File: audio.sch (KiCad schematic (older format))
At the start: 94 parts, among them CN1 LEFT_JOY, CN2 RIGHT_JOY, CN3 RIGHT, CN4 LEFT, Q301 2N3906, Q321 MPF102, Q331 MPF102, U14 LF347, U15 74LS157, U3 PAULA, U38 MC1488

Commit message: Almost there :)
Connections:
- net ~DKRD: now also R305.2
- net ~RXD: no longer R305.2
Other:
- moved on the sheet: R305
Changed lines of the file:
@@
 Sheet 5 14
 Title "Rämixx500"
-Date "2019-05-23"
+Date "2019-06-23"
 Rev "1git"
 Comp "SukkoPera"
@@
 ~INT2
 Wire Wire Line
-	3875 6155 4050 6155
-Wire Wire Line
 	3875 6305 4270 6305
 Text GLabel 4270 6155 2    50   Input ~ 0
@@
 ~TXD
 Wire Wire Line
-	3875 6705 4270 6705
+	3875 6705 4040 6705
 Wire Wire Line
 	3875 6855 4270 6855
@@
 L Device:R R305
 U 1 1 5E111042
-P 4300 5945
-F 0 "R305" V 4215 5845 50  0000 L CNN
-F 1 "1k" V 4300 5900 50  0000 L CNN
-F 2 "Raemixx500:R_Axial_DIN0309_L9.0mm_D3.2mm_P12.70mm_Horizontal" V 4230 5945 50  0001 C CNN
-F 3 "~" H 4300 5945 50  0001 C CNN
-	1    4300 5945
+P 4290 6495
+F 0 "R305" V 4205 6395 50  0000 L CNN
+F 1 "1k" V 4290 6450 50  0000 L CNN
+F 2 "Raemixx500:R_Axial_DIN0309_L9.0mm_D3.2mm_P12.70mm_Horizontal" V 4220 6495 50  0001 C CNN
+F 3 "~" H 4290 6495 50  0001 C CNN
+	1    4290 6495
 	0    1    1    0
 $EndComp
@@
 L power:VCC #PWR0159
 U 1 1 5E4D343F
-P 4650 5875
-F 0 "#PWR0159" H 4650 5725 50  0001 C CNN
-F 1 "VCC" H 4667 6048 50  0000 C CNN
-F 2 "" H 4650 5875 50  0001 C CNN
-F 3 "" H 4650 5875 50  0001 C CNN
-	1    4650 5875
-	1    0    0    -1
-$EndComp
-Wire Wire Line
-	4450 5945 4650 5945
-Wire Wire Line
-	4650 5945 4650 5875
-Wire Wire Line
-	4150 5945 4050 5945
-Wire Wire Line
-	4050 5945 4050 6155
-Connection ~ 4050 6155
-Wire Wire Line
-	4050 6155 4270 6155
+P 4640 6425
+F 0 "#PWR0159" H 4640 6275 50  0001 C CNN
+F 1 "VCC" H 4657 6598 50  0000 C CNN
+F 2 "" H 4640 6425 50  0001 C CNN
+F 3 "" H 4640 6425 50  0001 C CNN
+	1    4640 6425
+	1    0    0    -1
+$EndComp
+Wire Wire Line
+	4440 6495 4640 6495
+Wire Wire Line
+	4640 6495 4640 6425
+Wire Wire Line
+	4140 6495 4040 6495
+Wire Wire Line
+	4040 6495 4040 6705
 $Comp
 L Device:R R307
@@
 Wire Wire Line
 	5995 5030 7280 5030
+Connection ~ 4040 6705
+Wire Wire Line
+	4040 6705 4270 6705
+Wire Wire Line
+	3875 6155 4270 6155
 Wire Bus Line
 	1955 4305 1955 4505

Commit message: Fix shielding of D-Sub connectors
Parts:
- CN1, CN2: footprint w_conn_d-sub:DB_9M -> Raemixx500:DB_9M
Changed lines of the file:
@@
 F 0 "CN1" H 8775 1608 50  0000 C CNN
 F 1 "LEFT_JOY" H 8775 1699 50  0000 C CNN
-F 2 "w_conn_d-sub:DB_9M" H 8775 2300 50  0001 C CNN
+F 2 "Raemixx500:DB_9M" H 8775 2300 50  0001 C CNN
 F 3 " ~" H 8775 2300 50  0001 C CNN
 	1    8775 2300
@@
 F 0 "CN2" H 8775 3838 50  0000 C CNN
 F 1 "RIGHT_JOY" H 8775 3929 50  0000 C CNN
-F 2 "w_conn_d-sub:DB_9M" H 8775 4530 50  0001 C CNN
+F 2 "Raemixx500:DB_9M" H 8775 4530 50  0001 C CNN
 F 3 " ~" H 8775 4530 50  0001 C CNN
 	1    8775 4530

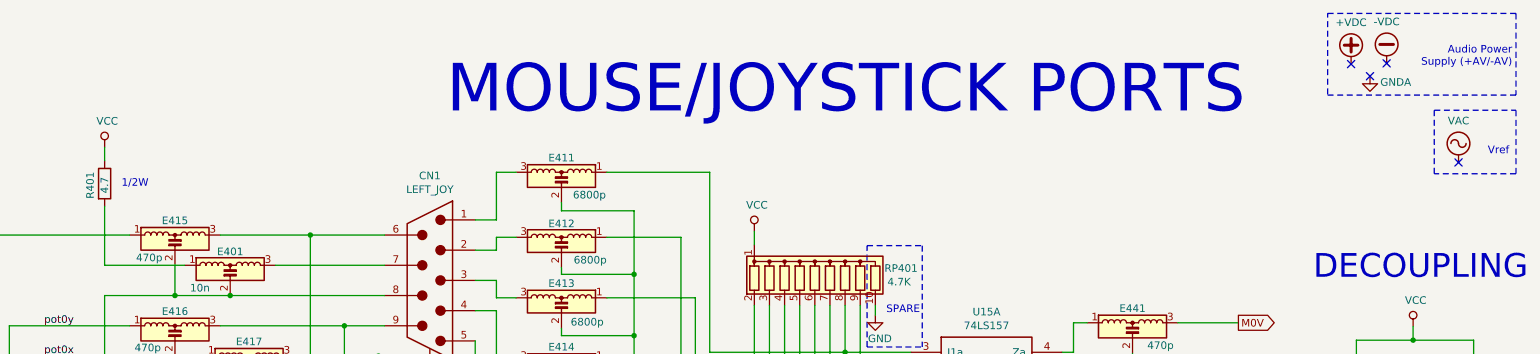
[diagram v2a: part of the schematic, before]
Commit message: Fix a lot of ERC/DRC errors
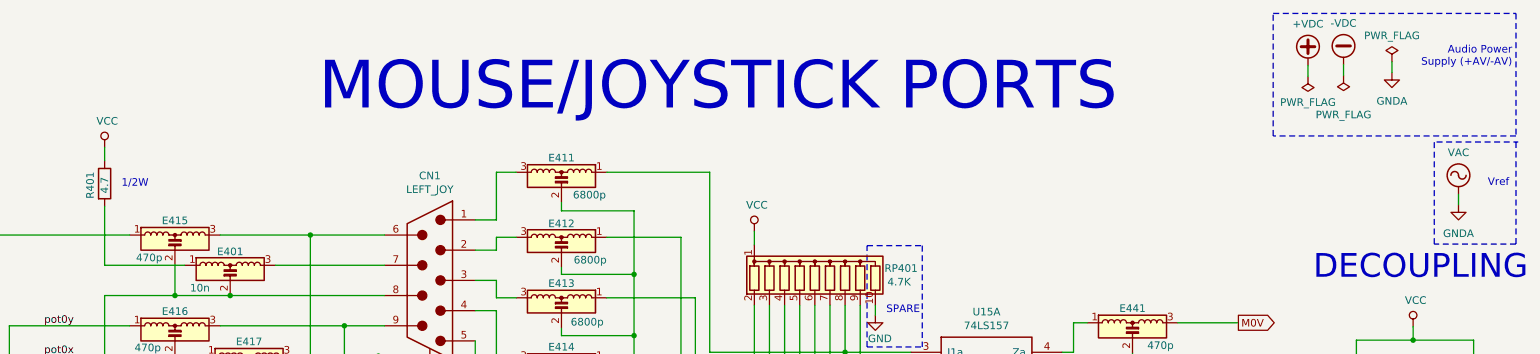
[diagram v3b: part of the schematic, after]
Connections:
- net VAC is gone; now on net GNDA: C305.1, C306.1, R303.1, R304.2, U14.10 (+), U14.12 (+)
- no-connect marks 4 -> 0
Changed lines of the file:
@@
 EESchema Schematic File Version 4
-LIBS:Raemix500-cache
-EELAYER 29 0
+EELAYER 30 0
 EELAYER END
 $Descr A3 16535 11693
@@
 Sheet 5 14
 Title "Rämixx500"
-Date "2019-06-23"
+Date "2020-04-04"
 Rev "1git"
 Comp "SukkoPera"
@@
 	1    0    0    -1
 $EndComp
-NoConn ~ 15100 865
 Text Notes 15930 890  2    50   ~ 0
 Audio Power\nSupply (+AV/-AV)
 Wire Notes Line
-	14710 535  15955 535
+	14350 535  15955 535
 Wire Notes Line
-	15955 535  15955 1075
+	15955 535  15955 1360
 Wire Notes Line
-	15955 1075 14710 1075
+	15955 1345 14350 1345
 Wire Notes Line
-	14710 1070 14710 535
+	14350 1345 14350 525
 $Comp
 L power:GNDA #PWR0132
 U 1 1 5D31919F
-P 14990 950
-F 0 "#PWR0132" H 14990 700 50  0001 C CNN
-F 1 "GNDA" H 15160 910 50  0000 C CNN
-F 2 "" H 14990 950 50  0001 C CNN
-F 3 "" H 14990 950 50  0001 C CNN
-	1    14990 950
-	1    0    0    -1
-$EndComp
-NoConn ~ 14990 950
+P 15135 925
+F 0 "#PWR0132" H 15135 675 50  0001 C CNN
+F 1 "GNDA" H 15135 735 50  0000 C CNN
+F 2 "" H 15135 925 50  0001 C CNN
+F 3 "" H 15135 925 50  0001 C CNN
+	1    15135 925
+	1    0    0    -1
+$EndComp
 $Comp
 L Device:EMI_Filter_LCL E416
@@
 L power:VAC #PWR0147
 U 1 1 5DBE05B3
-P 15575 1520
-F 0 "#PWR0147" H 15575 1420 50  0001 C CNN
-F 1 "VAC" H 15575 1795 50  0000 C CNN
-F 2 "" H 15575 1520 50  0001 C CNN
-F 3 "" H 15575 1520 50  0001 C CNN
-	1    15575 1520
-	1    0    0    -1
-$EndComp
-NoConn ~ 15575 1520
-Text Notes 15910 1475 2    50   ~ 0
+P 15575 1730
+F 0 "#PWR0147" H 15575 1630 50  0001 C CNN
+F 1 "VAC" H 15575 2005 50  0000 C CNN
+F 2 "" H 15575 1730 50  0001 C CNN
+F 3 "" H 15575 1730 50  0001 C CNN
+	1    15575 1730
+	1    0    0    -1
+$EndComp
+Text Notes 15910 1685 2    50   ~ 0
 Vref
 $Comp
@@
 Text Notes 15090 6570 2    315  ~ 0
 AUDIO FILTERS
-Text Notes 14165 1225 2    315  ~ 0
+Text Notes 13320 1205 2    315  ~ 0
 MOUSE/JOYSTICK PORTS
 $Comp
@@
 	6870 6920 7175 6920
 Wire Notes Line
-	15415 1175 15955 1175
+	15430 1385 15970 1385
 Wire Notes Line
-	15955 1175 15955 1595
+	15955 1385 15955 2075
 Wire Notes Line
-	15955 1595 15415 1595
+	15955 2060 15415 2060
 Wire Notes Line
-	15415 1595 15415 1175
+	15415 2060 15415 1385
 Text Notes 9045 10220 2    50   ~ 0
 This whole circuit has some\ndifferent values on A600.
@@
 L power:-VDC #PWR0216
 U 1 1 5DF41869
-P 15100 865
-F 0 "#PWR0216" H 15100 765 50  0001 C CNN
-F 1 "-VDC" H 15100 1140 50  0000 C CNN
-F 2 "" H 15100 865 50  0001 C CNN
-F 3 "" H 15100 865 50  0001 C CNN
-	1    15100 865
+P 14815 875
+F 0 "#PWR0216" H 14815 775 50  0001 C CNN
+F 1 "-VDC" H 14815 1150 50  0000 C CNN
+F 2 "" H 14815 875 50  0001 C CNN
+F 3 "" H 14815 875 50  0001 C CNN
+	1    14815 875
 	1    0    0    -1
 $EndComp
@@
 L power:+VDC #PWR0217
 U 1 1 5DF419B8
-P 14865 870
-F 0 "#PWR0217" H 14865 770 50  0001 C CNN
-F 1 "+VDC" H 14865 1145 50  0000 C CNN
-F 2 "" H 14865 870 50  0001 C CNN
-F 3 "" H 14865 870 50  0001 C CNN
-	1    14865 870
-	1    0    0    -1
-$EndComp
-NoConn ~ 14865 870
+P 14580 880
+F 0 "#PWR0217" H 14580 780 50  0001 C CNN
+F 1 "+VDC" H 14580 1155 50  0000 C CNN
+F 2 "" H 14580 880 50  0001 C CNN
+F 3 "" H 14580 880 50  0001 C CNN
+	1    14580 880
+	1    0    0    -1
+$EndComp
 $Comp
 L power:-VDC #PWR0218
@@
 Wire Wire Line
 	3875 6155 4270 6155
+$Comp
+L power:PWR_FLAG #FLG0103
+U 1 1 5EE75F30
+P 15135 855
+F 0 "#FLG0103" H 15135 930 50  0001 C CNN
+F 1 "PWR_FLAG" H 15135 1028 50  0000 C CNN
+F 2 "" H 15135 855 50  0001 C CNN
+F 3 "~" H 15135 855 50  0001 C CNN
+	1    15135 855
+	1    0    0    -1
+$EndComp
+Wire Wire Line
+	15135 925  15135 855
+$Comp
+L power:PWR_FLAG #FLG0104
+U 1 1 5EF3EBCB
+P 14815 945
+F 0 "#FLG0104" H 14815 1020 50  0001 C CNN
+F 1 "PWR_FLAG" H 14815 1205 50  0000 C CNN
+F 2 "" H 14815 945 50  0001 C CNN
+F 3 "~" H 14815 945 50  0001 C CNN
+	1    14815 945
+	-1   0    0    1
+$EndComp
+Wire Wire Line
+	14815 875  14815 945
+$Comp
+L power:PWR_FLAG #FLG0105
+U 1 1 5EF849F2
+P 14580 950
+F 0 "#FLG0105" H 14580 1025 50  0001 C CNN
+F 1 "PWR_FLAG" H 14580 1123 50  0000 C CNN
+F 2 "" H 14580 950 50  0001 C CNN
+F 3 "~" H 14580 950 50  0001 C CNN
+	1    14580 950
+	-1   0    0    1
+$EndComp
+Wire Wire Line
+	14580 880  14580 950
+$Comp
+L power:GNDA #PWR0270
+U 1 1 5F2DFC32
+P 15575 1800
+F 0 "#PWR0270" H 15575 1550 50  0001 C CNN
+F 1 "GNDA" H 15575 1610 50  0000 C CNN
+F 2 "" H 15575 1800 50  0001 C CNN
+F 3 "" H 15575 1800 50  0001 C CNN
+	1    15575 1800
+	1    0    0    -1
+$EndComp
+Wire Wire Line
+	15575 1800 15575 1730
 Wire Bus Line
 	1955 4305 1955 4505

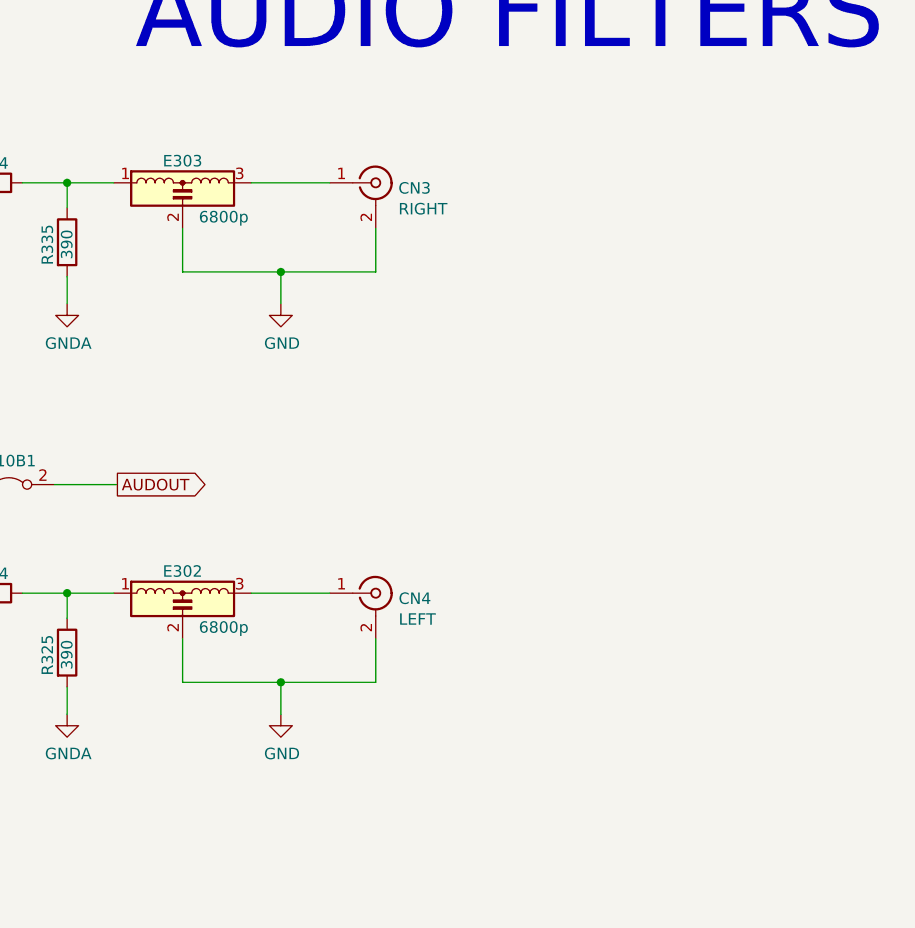
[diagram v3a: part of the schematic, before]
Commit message: Replace audio/composite jacks with A600's - This means PCB IS READY! Still need to fix the silkscreen though...
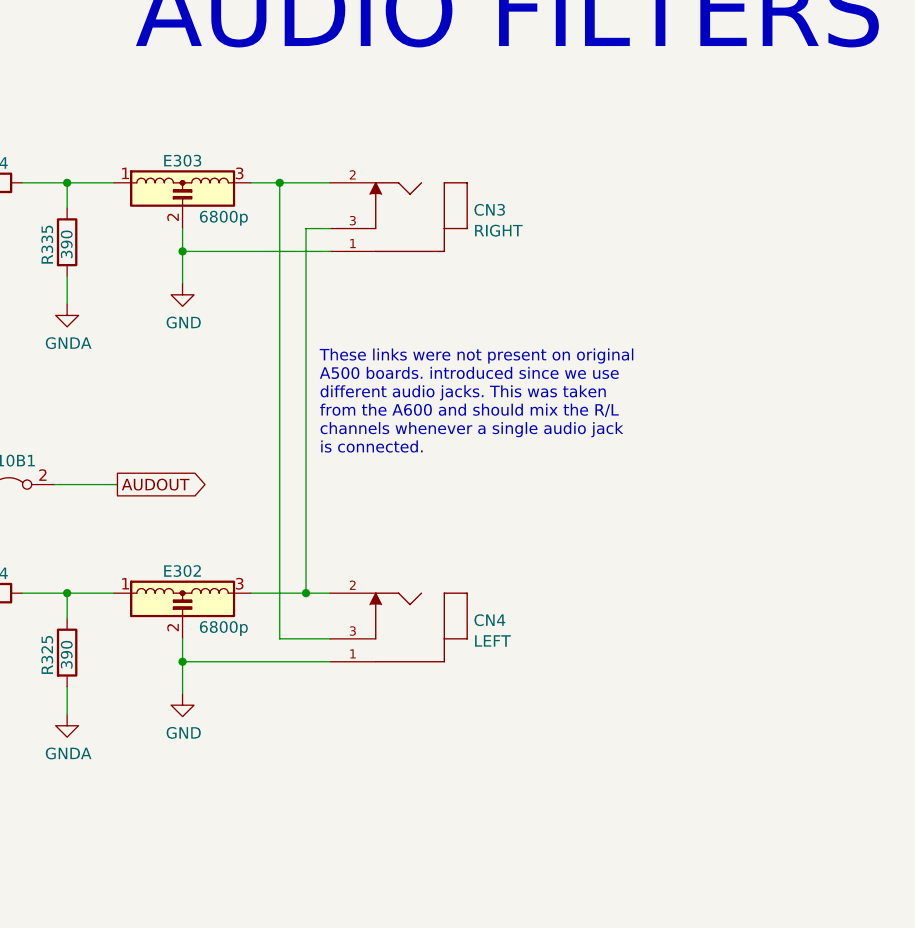
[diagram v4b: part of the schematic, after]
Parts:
- removed CN3: RIGHT, w_conn_av:rca_red, symbol Connector:Conn_Coaxial
- removed CN4: LEFT, w_conn_av:rca_white, symbol Connector:Conn_Coaxial
- added CN3: RIGHT, Raemixx500:SWITCHCRAFT_PJRAN1X1U01X, symbol PJRAN1X1U01X:PJRAN1X1U01X
- added CN4: LEFT, Raemixx500:SWITCHCRAFT_PJRAN1X1U01X, symbol PJRAN1X1U01X:PJRAN1X1U01X
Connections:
- net GND: now also CN3.1, CN4.1
- net at E302.3: now also CN3.3, CN4.2
- net at E303.3: now also CN3.2, CN4.3
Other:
- note added: "These links were not present on original\nA500 boards. introduced since we use\ndifferent audio jacks. This was taken\nfrom the A600 and should mix the R/L\nchannels whenever a single audio jack\nis connected."
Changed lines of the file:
@@
 Wire Wire Line
 	11515 9445 11515 9325
-$Comp
-L Connector:Conn_Coaxial CN4
-U 1 1 5DB6BA04
-P 12865 8915
-F 0 "CN4" H 12965 8891 50  0000 L CNN
-F 1 "LEFT" H 12965 8800 50  0000 L CNN
-F 2 "w_conn_av:rca_white" H 12865 8915 50  0001 C CNN
-F 3 " ~" H 12865 8915 50  0001 C CNN
-	1    12865 8915
-	1    0    0    -1
-$EndComp
-Wire Wire Line
-	12020 9115 12020 9305
-Wire Wire Line
-	12020 9305 12450 9305
-Wire Wire Line
-	12865 9305 12865 9115
-$Comp
-L power:GND #PWR0146
-U 1 1 5DB828C1
-P 12450 9445
-F 0 "#PWR0146" H 12450 9195 50  0001 C CNN
-F 1 "GND" H 12455 9272 50  0000 C CNN
-F 2 "" H 12450 9445 50  0001 C CNN
-F 3 "" H 12450 9445 50  0001 C CNN
-	1    12450 9445
-	1    0    0    -1
-$EndComp
-Wire Wire Line
-	12450 9445 12450 9305
-Connection ~ 12450 9305
-Wire Wire Line
-	12450 9305 12865 9305
-Wire Wire Line
-	12320 8915 12665 8915
+Wire Wire Line
+	12020 9115 12020 9215
 $Comp
 L power:VAC #PWR0147
@@
 Wire Wire Line
 	11515 7650 11515 7530
-$Comp
-L Connector:Conn_Coaxial CN3
-U 1 1 5DD9A1DF
-P 12865 7120
-F 0 "CN3" H 12964 7096 50  0000 L CNN
-F 1 "RIGHT" H 12964 7005 50  0000 L CNN
-F 2 "w_conn_av:rca_red" H 12865 7120 50  0001 C CNN
-F 3 " ~" H 12865 7120 50  0001 C CNN
-	1    12865 7120
-	1    0    0    -1
-$EndComp
-Wire Wire Line
-	12020 7320 12020 7510
-Wire Wire Line
-	12020 7510 12450 7510
-Wire Wire Line
-	12865 7510 12865 7320
-$Comp
-L power:GND #PWR0151
-U 1 1 5DD9A1E8
-P 12450 7650
-F 0 "#PWR0151" H 12450 7400 50  0001 C CNN
-F 1 "GND" H 12455 7477 50  0000 C CNN
-F 2 "" H 12450 7650 50  0001 C CNN
-F 3 "" H 12450 7650 50  0001 C CNN
-	1    12450 7650
-	1    0    0    -1
-$EndComp
-Wire Wire Line
-	12450 7650 12450 7510
-Connection ~ 12450 7510
-Wire Wire Line
-	12450 7510 12865 7510
-Wire Wire Line
-	12320 7120 12665 7120
+Wire Wire Line
+	12320 7120 12445 7120
 $Comp
 L power:VAC #PWR0152
@@
 Wire Wire Line
 	15575 1800 15575 1730
+$Comp
+L PJRAN1X1U01X:PJRAN1X1U01X CN3
+U 1 1 5F7C1CDB
+P 12965 7320
+F 0 "CN3" H 12637 7400 50  0000 R CNN
+F 1 "RIGHT" H 12637 7309 50  0000 R CNN
+F 2 "Raemixx500:SWITCHCRAFT_PJRAN1X1U01X" H 12965 7320 50  0001 L BNN
+F 3 "A" H 12965 7320 50  0001 L BNN
+F 4 "Switchcraft" H 12965 7320 50  0001 L BNN "Field4"
+F 5 "13mm" H 12965 7320 50  0001 L BNN "Field5"
+F 6 "Manufacturer Recommendations" H 12965 7320 50  0001 L BNN "Field6"
+	1    12965 7320
+	-1   0    0    -1
+$EndComp
+Wire Wire Line
+	12320 8915 12560 8915
+$Comp
+L PJRAN1X1U01X:PJRAN1X1U01X CN4
+U 1 1 5FA7359A
+P 12965 9115
+F 0 "CN4" H 12637 9195 50  0000 R CNN
+F 1 "LEFT" H 12637 9104 50  0000 R CNN
+F 2 "Raemixx500:SWITCHCRAFT_PJRAN1X1U01X" H 12965 9115 50  0001 L BNN
+F 3 "A" H 12965 9115 50  0001 L BNN
+F 4 "Switchcraft" H 12965 9115 50  0001 L BNN "Field4"
+F 5 "13mm" H 12965 9115 50  0001 L BNN "Field5"
+F 6 "Manufacturer Recommendations" H 12965 9115 50  0001 L BNN "Field6"
+	1    12965 9115
+	-1   0    0    -1
+$EndComp
+Wire Wire Line
+	12020 9355 12020 9215
+$Comp
+L power:GND #PWR0146
+U 1 1 5FA735A5
+P 12020 9355
+F 0 "#PWR0146" H 12020 9105 50  0001 C CNN
+F 1 "GND" H 12025 9182 50  0000 C CNN
+F 2 "" H 12020 9355 50  0001 C CNN
+F 3 "" H 12020 9355 50  0001 C CNN
+	1    12020 9355
+	1    0    0    -1
+$EndComp
+Wire Wire Line
+	12665 7320 12560 7320
+Wire Wire Line
+	12560 7320 12560 8915
+Connection ~ 12560 8915
+Wire Wire Line
+	12560 8915 12665 8915
+Connection ~ 12020 9215
+Wire Wire Line
+	12020 9215 12665 9215
+Wire Wire Line
+	12020 7320 12020 7420
+$Comp
+L power:GND #PWR0151
+U 1 1 5DD9A1E8
+P 12020 7560
+F 0 "#PWR0151" H 12020 7310 50  0001 C CNN
+F 1 "GND" H 12025 7387 50  0000 C CNN
+F 2 "" H 12020 7560 50  0001 C CNN
+F 3 "" H 12020 7560 50  0001 C CNN
+	1    12020 7560
+	1    0    0    -1
+$EndComp
+Wire Wire Line
+	12020 7560 12020 7420
+Connection ~ 12020 7420
+Wire Wire Line
+	12020 7420 12665 7420
+Wire Wire Line
+	12665 9115 12445 9115
+Wire Wire Line
+	12445 9115 12445 7120
 Wire Bus Line
 	1955 4305 1955 4505
@@
 Wire Bus Line
 	1955 4705 1955 6205
+Connection ~ 12445 7120
+Wire Wire Line
+	12445 7120 12665 7120
+Text Notes 12620 8315 0    50   ~ 0
+These links were not present on original\nA500 boards. introduced since we use\ndifferent audio jacks. This was taken\nfrom the A600 and should mix the R/L\nchannels whenever a single audio jack\nis connected.
 $EndSCHEMATC

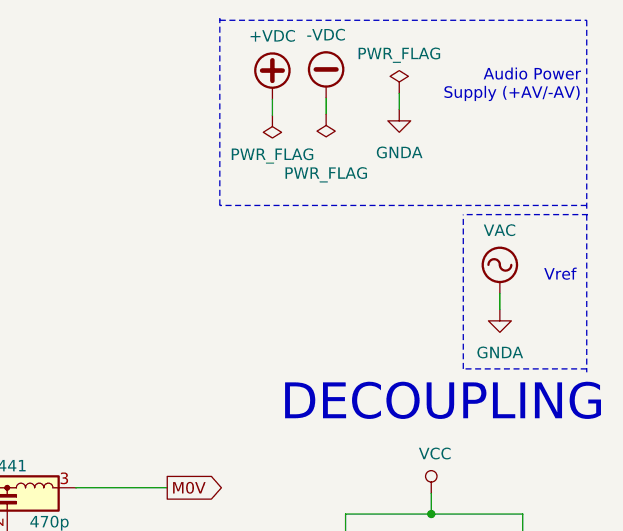
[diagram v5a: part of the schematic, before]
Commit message: Erm, fix a huge mistake in the audio part and some refinements
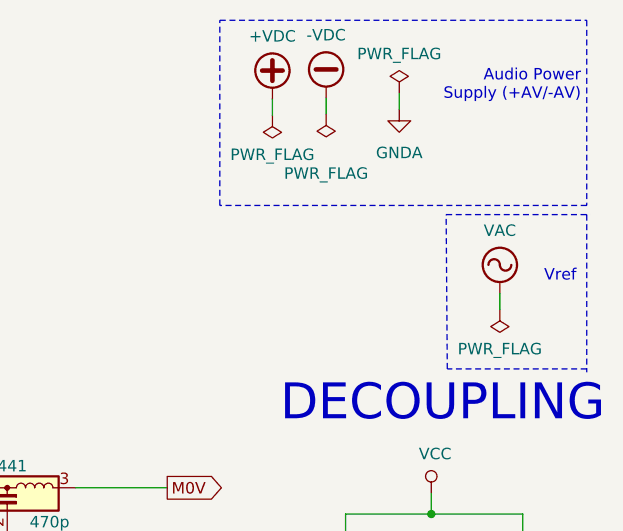
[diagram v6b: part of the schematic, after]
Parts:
- C303, C304: footprint Capacitor_THT:CP_Radial_D5.0mm_P2.00mm -> Capacitor_THT:CP_Radial_D5.0mm_P2.50mm
- C306: footprint Capacitor_THT:CP_Radial_D8.0mm_P5.00mm -> Capacitor_THT:CP_Radial_D5.0mm_P2.50mm
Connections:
- net GNDA: no longer C305.1, C306.1, R303.1, R304.2, U14.10 (+), U14.12 (+)
- new net VAC: C305.1, C306.1, R303.1, R304.2, U14.10 (+), U14.12 (+)
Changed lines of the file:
@@
 	14350 535  15955 535
 Wire Notes Line
-	15955 535  15955 1360
+	15955 535  15955 1345
 Wire Notes Line
 	15955 1345 14350 1345
 Wire Notes Line
-	14350 1345 14350 525
+	14350 1345 14350 535
 $Comp
 L power:GNDA #PWR0132
@@
 	6870 6920 7175 6920
 Wire Notes Line
-	15430 1385 15970 1385
+	15340 1385 15970 1385
 Wire Notes Line
 	15955 1385 15955 2075
 Wire Notes Line
-	15955 2060 15415 2060
+	15955 2060 15345 2060
 Wire Notes Line
-	15415 2060 15415 1385
+	15345 2060 15340 1385
 Text Notes 9045 10220 2    50   ~ 0
 This whole circuit has some\ndifferent values on A600.
@@
 F 0 "C306" H 4380 2161 50  0000 L CNN
 F 1 "10u" H 4380 2070 50  0000 L CNN
-F 2 "Capacitor_THT:CP_Radial_D8.0mm_P5.00mm" H 4265 2115 50  0001 C CNN
+F 2 "Capacitor_THT:CP_Radial_D5.0mm_P2.50mm" H 4265 2115 50  0001 C CNN
 F 3 "~" H 4265 2115 50  0001 C CNN
 	1    4265 2115
@@
 F 0 "C303" H 2175 9561 50  0000 L CNN
 F 1 "22u" H 2175 9470 50  0000 L CNN
-F 2 "Capacitor_THT:CP_Radial_D5.0mm_P2.00mm" H 2060 9515 50  0001 C CNN
+F 2 "Capacitor_THT:CP_Radial_D5.0mm_P2.50mm" H 2060 9515 50  0001 C CNN
 F 3 "~" H 2060 9515 50  0001 C CNN
 	1    2060 9515
@@
 F 0 "C304" H 2175 9946 50  0000 L CNN
 F 1 "22u" H 2175 9855 50  0000 L CNN
-F 2 "Capacitor_THT:CP_Radial_D5.0mm_P2.00mm" H 2060 9900 50  0001 C CNN
+F 2 "Capacitor_THT:CP_Radial_D5.0mm_P2.50mm" H 2060 9900 50  0001 C CNN
 F 3 "~" H 2060 9900 50  0001 C CNN
 	1    2060 9900
@@
 Wire Wire Line
 	14580 880  14580 950
-$Comp
-L power:GNDA #PWR0270
-U 1 1 5F2DFC32
-P 15575 1800
-F 0 "#PWR0270" H 15575 1550 50  0001 C CNN
-F 1 "GNDA" H 15575 1610 50  0000 C CNN
-F 2 "" H 15575 1800 50  0001 C CNN
-F 3 "" H 15575 1800 50  0001 C CNN
-	1    15575 1800
-	1    0    0    -1
-$EndComp
 Wire Wire Line
 	15575 1800 15575 1730
@@
 Text Notes 12620 8315 0    50   ~ 0
 These links were not present on original\nA500 boards. introduced since we use\ndifferent audio jacks. This was taken\nfrom the A600 and should mix the R/L\nchannels whenever a single audio jack\nis connected.
+$Comp
+L power:PWR_FLAG #FLG0109
+U 1 1 5EE25C45
+P 15575 1800
+F 0 "#FLG0109" H 15575 1875 50  0001 C CNN
+F 1 "PWR_FLAG" H 15575 1973 50  0000 C CNN
+F 2 "" H 15575 1800 50  0001 C CNN
+F 3 "~" H 15575 1800 50  0001 C CNN
+	1    15575 1800
+	-1   0    0    1
+$EndComp
 Wire Bus Line
 	1955 4305 1955 4505
